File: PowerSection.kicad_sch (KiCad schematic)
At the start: 16 parts, among them J2 B2B-PH-SM4-TBLFSN, J3 USB_B_Micro, U3 TPS62840DLCR, U4 MCP73831T-2ACI_OT

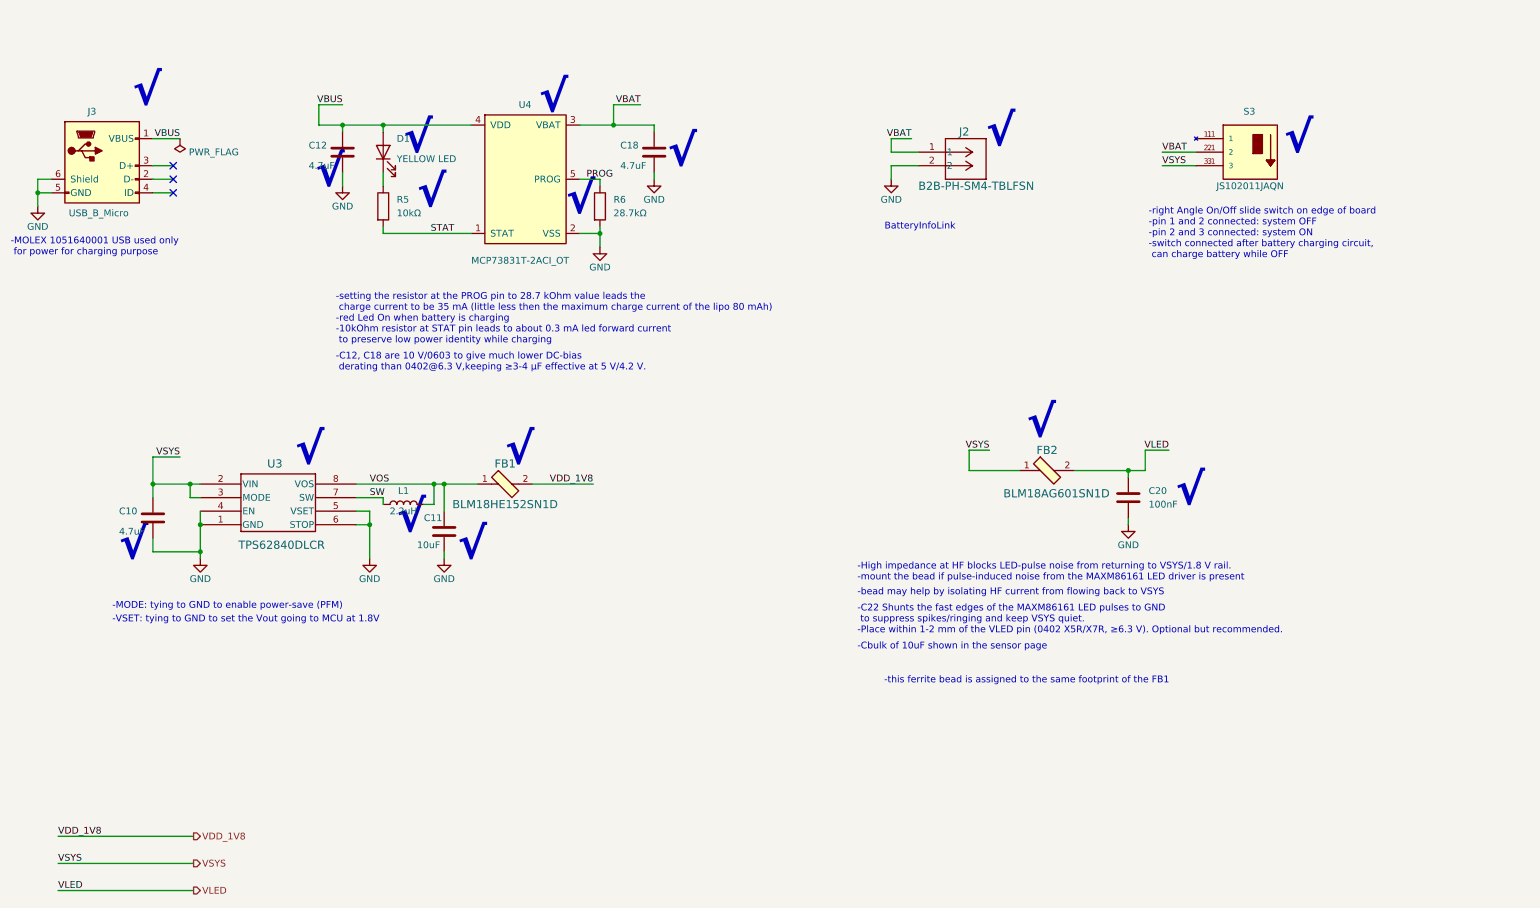
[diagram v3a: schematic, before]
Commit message: finished layout, associated 3d models for the components, drc ran with no errors. fixed foorprints and their individaul pad dimensions (solder mask layer related, copper layer related and paste mask layer related) . EUROCIRCUITS Manufacturer report resulted in class 4C , standard and towards low cost. still needs to fix and revise silkscreen and fabrication layer
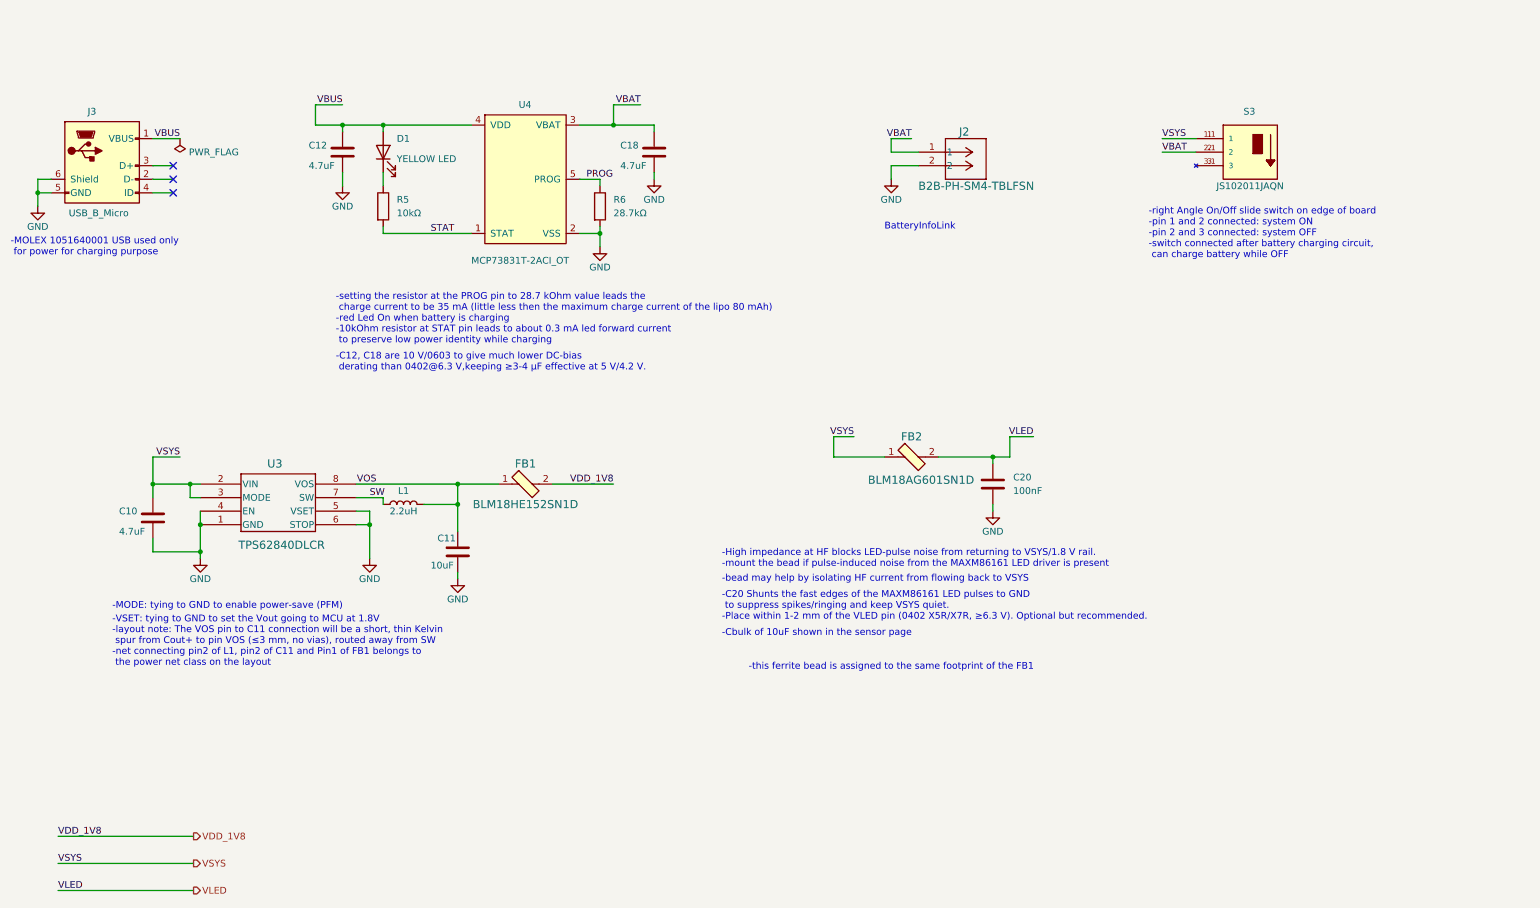
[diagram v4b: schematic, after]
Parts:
- J2: footprint ul_BatteryConnector_B2B-PH-SM4-TB-LF-SN_local:CONN_B2B-PH-SM4-TBLFSN_JST -> ul_BatteryConnector_S2B-PH-SM4-TB_local:CONN_S2B-PH-SM4-TB_JST
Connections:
- net VSYS: now also S3.1, S3.1.1 (1); no longer S3.3, S3.3.1 (3)
- new net: S3.3, S3.3.1 (3)
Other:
- note added: "-C20 Shunts the fast edges of the MAXM86161 LED pulses to GND to suppress spikes/ringing and keep VSYS quiet. -Place within 1-2 mm of the VLED pin (0402 X5R/X7R, ≥6.3 V). Optional but recommended."
- note added: "-layout note: The VOS pin to C11 connection will be a short, thin Kelvin spur from Cout+ to pin VOS (≤3 mm, no vias), routed away from SW -net connecting pin2 of L1, pin2 of C11 and Pin1 of FB1 belongs to the power net class on the layout"
- note added: "-right Angle On/Off slide switch on edge of board -pin 1 and 2 connected: system ON -pin 2 and 3 connected: system OFF -switch connected after battery charging circuit, can charge battery while OFF"
- note removed: "-C22 Shunts the fast edges of the MAXM86161 LED pulses to GND to suppress spikes/ringing and keep VSYS quiet. -Place within 1-2 mm of the VLED pin (0402 X5R/X7R, ≥6.3 V). Optional but recommended."
- note removed: "-right Angle On/Off slide switch on edge of board -pin 1 and 2 connected: system OFF -pin 2 and 3 connected: system ON -switch connected after battery charging circuit, can charge battery while OFF"
- note removed: "√"
- moved on the sheet: C11, C20, FB1, FB2
